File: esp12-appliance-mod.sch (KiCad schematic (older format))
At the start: 32 parts, among them J1 CONN2, J2 CONN6, J3 CONN2, J4 CONN2, J5 CONN2, J6 CONN2, J7 CONN2, K1 RELAY_TE_RE314F05, Q1 MMBT4401, Q2 MMBT4401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

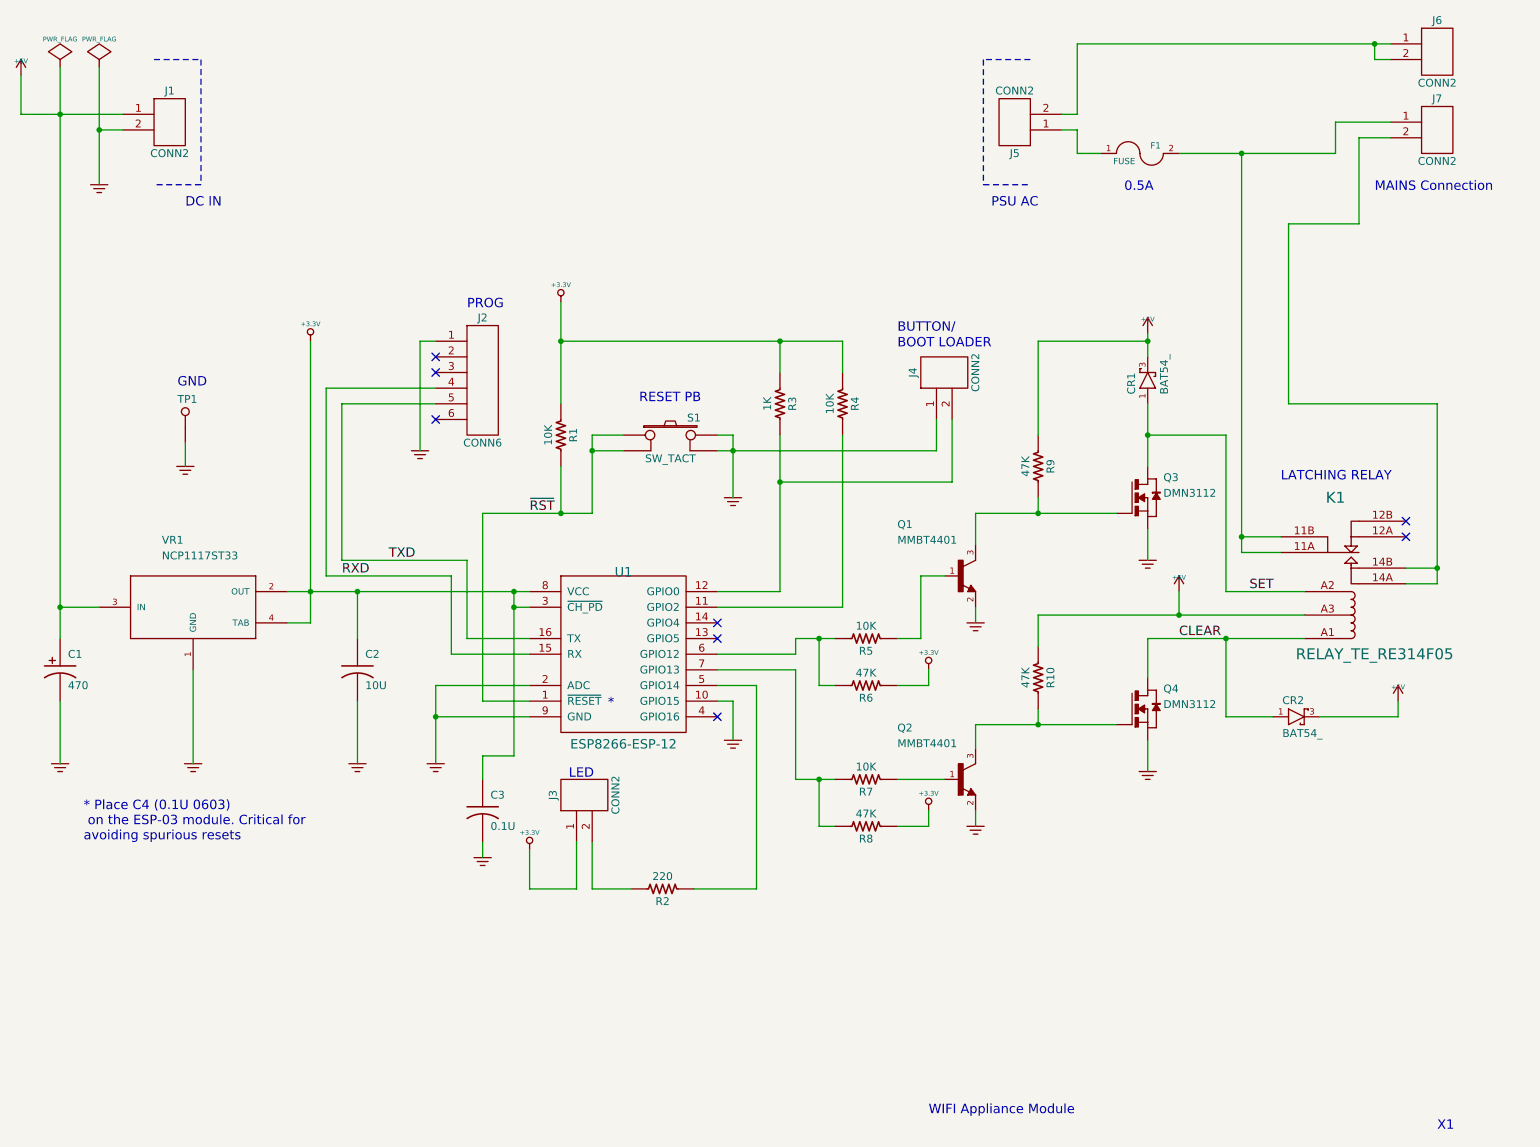
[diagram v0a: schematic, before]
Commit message: Add part numbers to schematic. Regenerate BOM using BOMTools
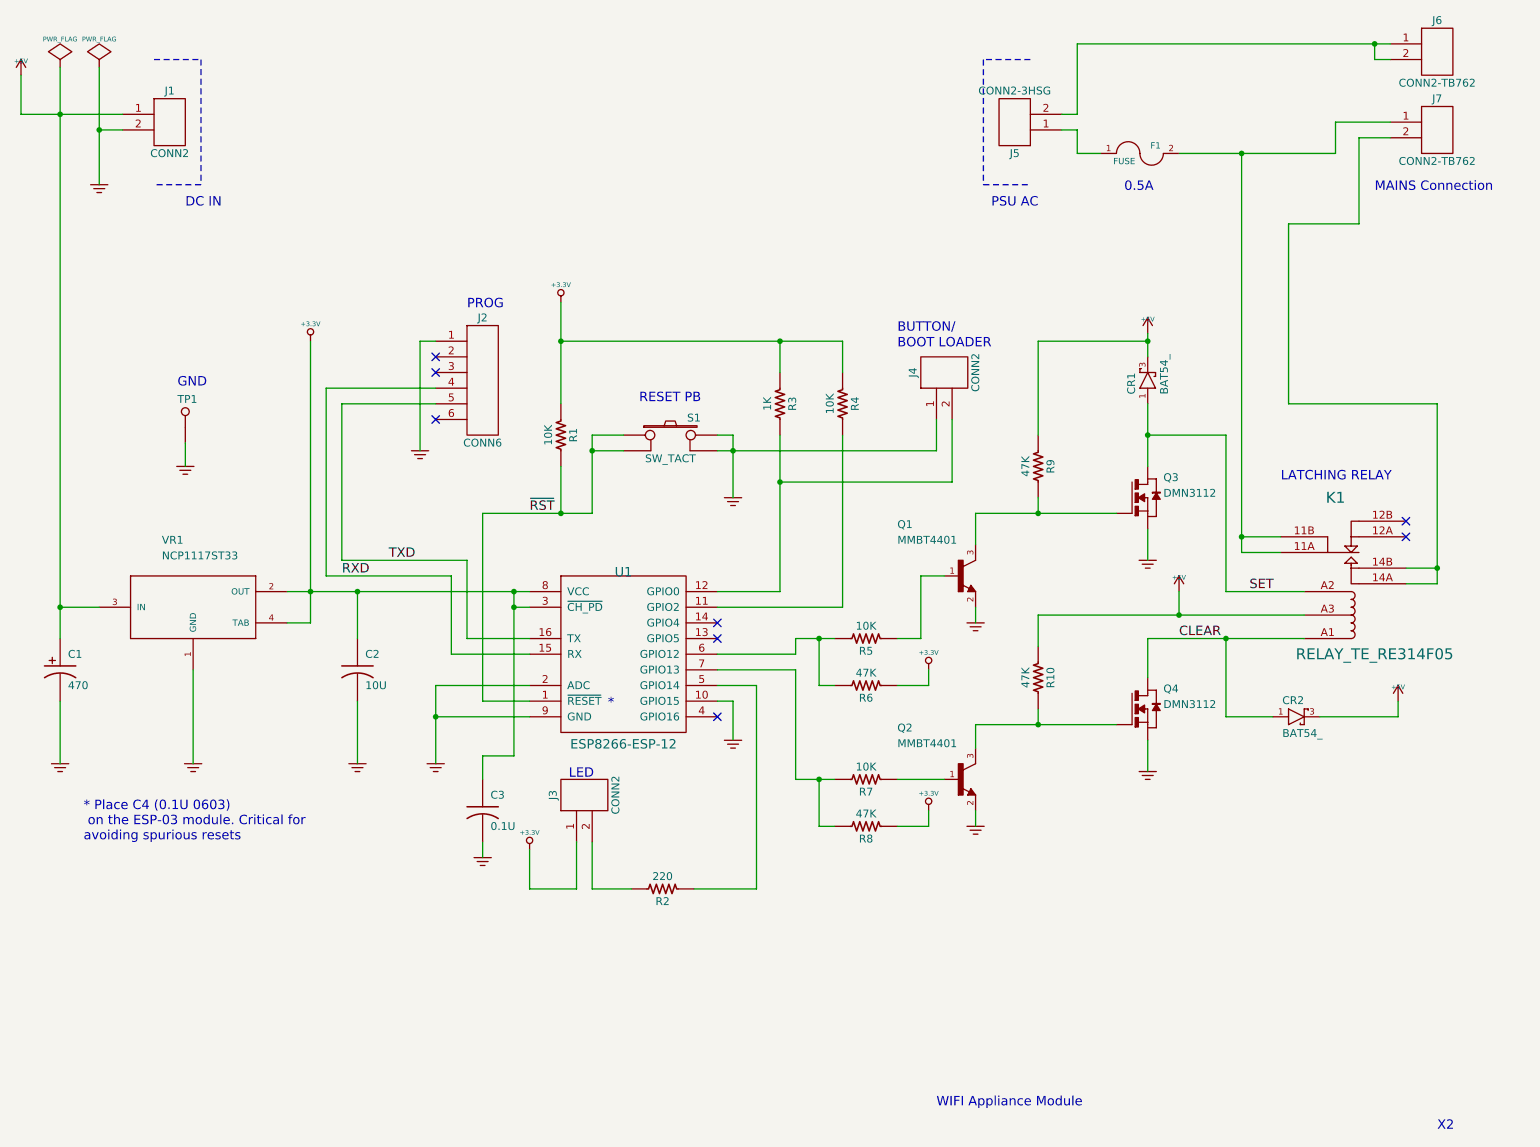
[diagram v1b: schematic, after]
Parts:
- C1: PartNumber (none) -> 800126-477
- C2: PartNumber (none) -> 800003-106
- C3: PartNumber (none) -> 800000-104
- CR1, CR2: PartNumber (none) -> 800127-101
- F1: PartNumber (none) -> 800125-500
- J1, J3, J4: PartNumber (none) -> 800114-102
- J2: PartNumber (none) -> 800116-106
- J5: value CONN2 -> CONN2-3HSG; PartNumber (none) -> 800124-101
- J6, J7: value CONN2 -> CONN2-TB762; PartNumber (none) -> 800129-102
- K1: PartNumber (none) -> 800128-101
- Q1, Q2: PartNumber (none) -> 800110-101
- Q3, Q4: PartNumber (none) -> 800123-101
- R1, R4, R5, R7: PartNumber (none) -> 800010-103
- R2: footprint RC0603 -> RC0805; PartNumber (none) -> 800011-221
- R3: PartNumber (none) -> 800010-102
- R6, R8, R9: PartNumber (none) -> 800010-473
- S1: PartNumber (none) -> 800107-101
- U1: PartNumber (none) -> 800106-101
- VR1: PartNumber (none) -> 800121-101
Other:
- note added: "X2"
- note removed: "X1"
